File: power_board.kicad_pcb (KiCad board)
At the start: 2 copper layers, 156 x 90 mm, 110 parts, among them J1 Conn_01x01, J10 Conn_01x02, J11 Conn_01x02, J12 Conn_01x02, J13 Conn_01x02, J14 Conn_01x02, J15 Conn_01x02, J16 Conn_01x02, J17 Conn_01x02, J18 Conn_01x02, J19 Conn_01x02, J2 Conn_01x01, J20 Conn_01x03, J21 Conn_01x03, J22 Conn_01x03, J23 Conn_01x03, J24 Conn_01x03, J25 Conn_01x02, J26 Conn_01x02, J27 Conn_01x02, J28 Conn_01x02, J29 Conn_01x02, J3 Conn_01x01, J30 Conn_01x02, J4 ATX-24, J5 Conn_01x02, J6 Conn_01x02, J7 Conn_01x02, J8 Conn_01x02, J9 Conn_01x02, K1 SANYOU_SRD_Form_C, K2 SANYOU_SRD_Form_C, K3 SANYOU_SRD_Form_C, K4 SANYOU_SRD_Form_C, K5 SANYOU_SRD_Form_C, Q1 MMBT4401-7-F, Q10 MMBT4401-7-F, Q11 SI7113ADN-T1-GE3, Q12 Q_NMOS_GDS, Q13 Q_NMOS_GDS, Q14 Q_NMOS_GDS, Q15 Q_NMOS_GDS, Q16 Q_NMOS_GDS, Q2 MMBT4401-7-F, Q3 MMBT4401-7-F, Q4 SI7113ADN-T1-GE3, Q5 SI7113ADN-T1-GE3, Q6 MMBT4401-7-F, Q7 MMBT4401-7-F, Q8 SI7113ADN-T1-GE3, Q9 SI7113ADN-T1-GE3, U1 PCA9685PW, U2 PCA9685PW, U3 L298HN, U4 l6210, U5 L298HN, U6 l6210, U7 L298HN, U8 l6210

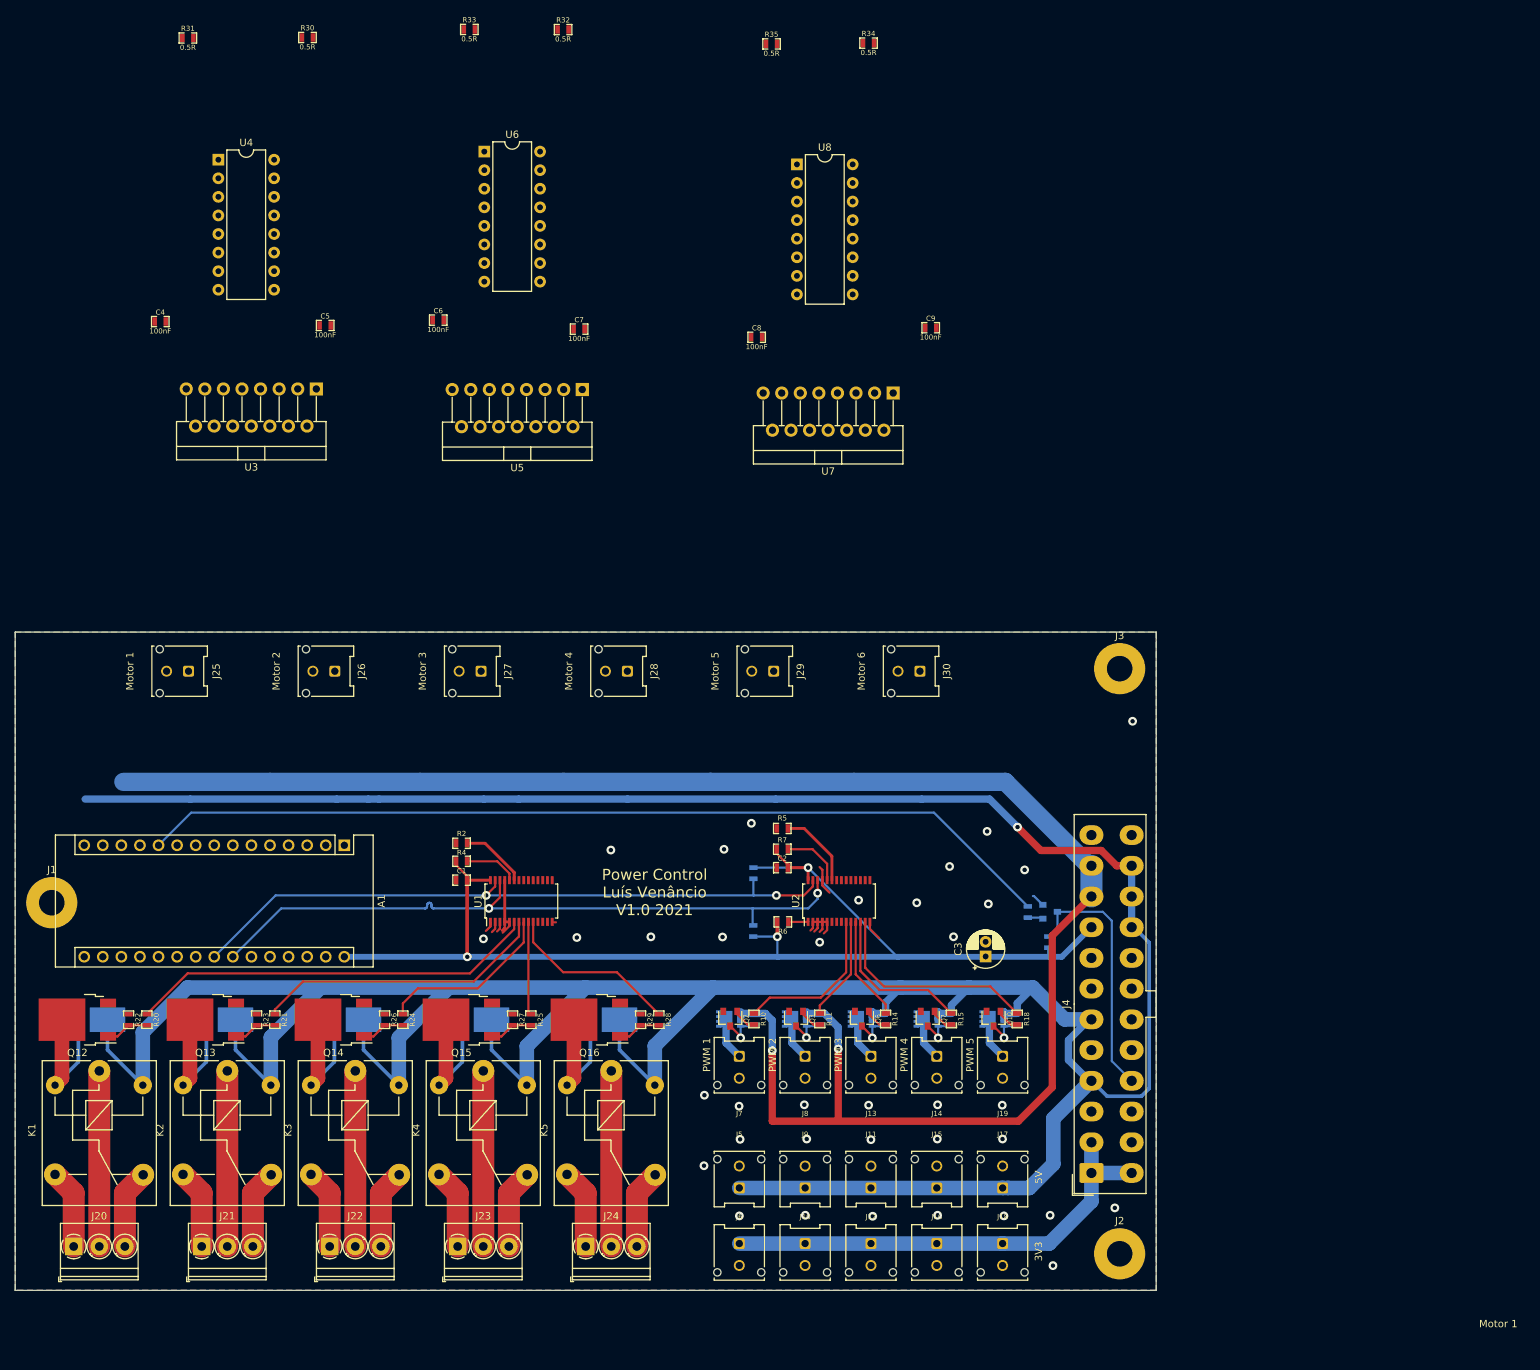
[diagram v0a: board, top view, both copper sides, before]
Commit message: Replaced driver footprints
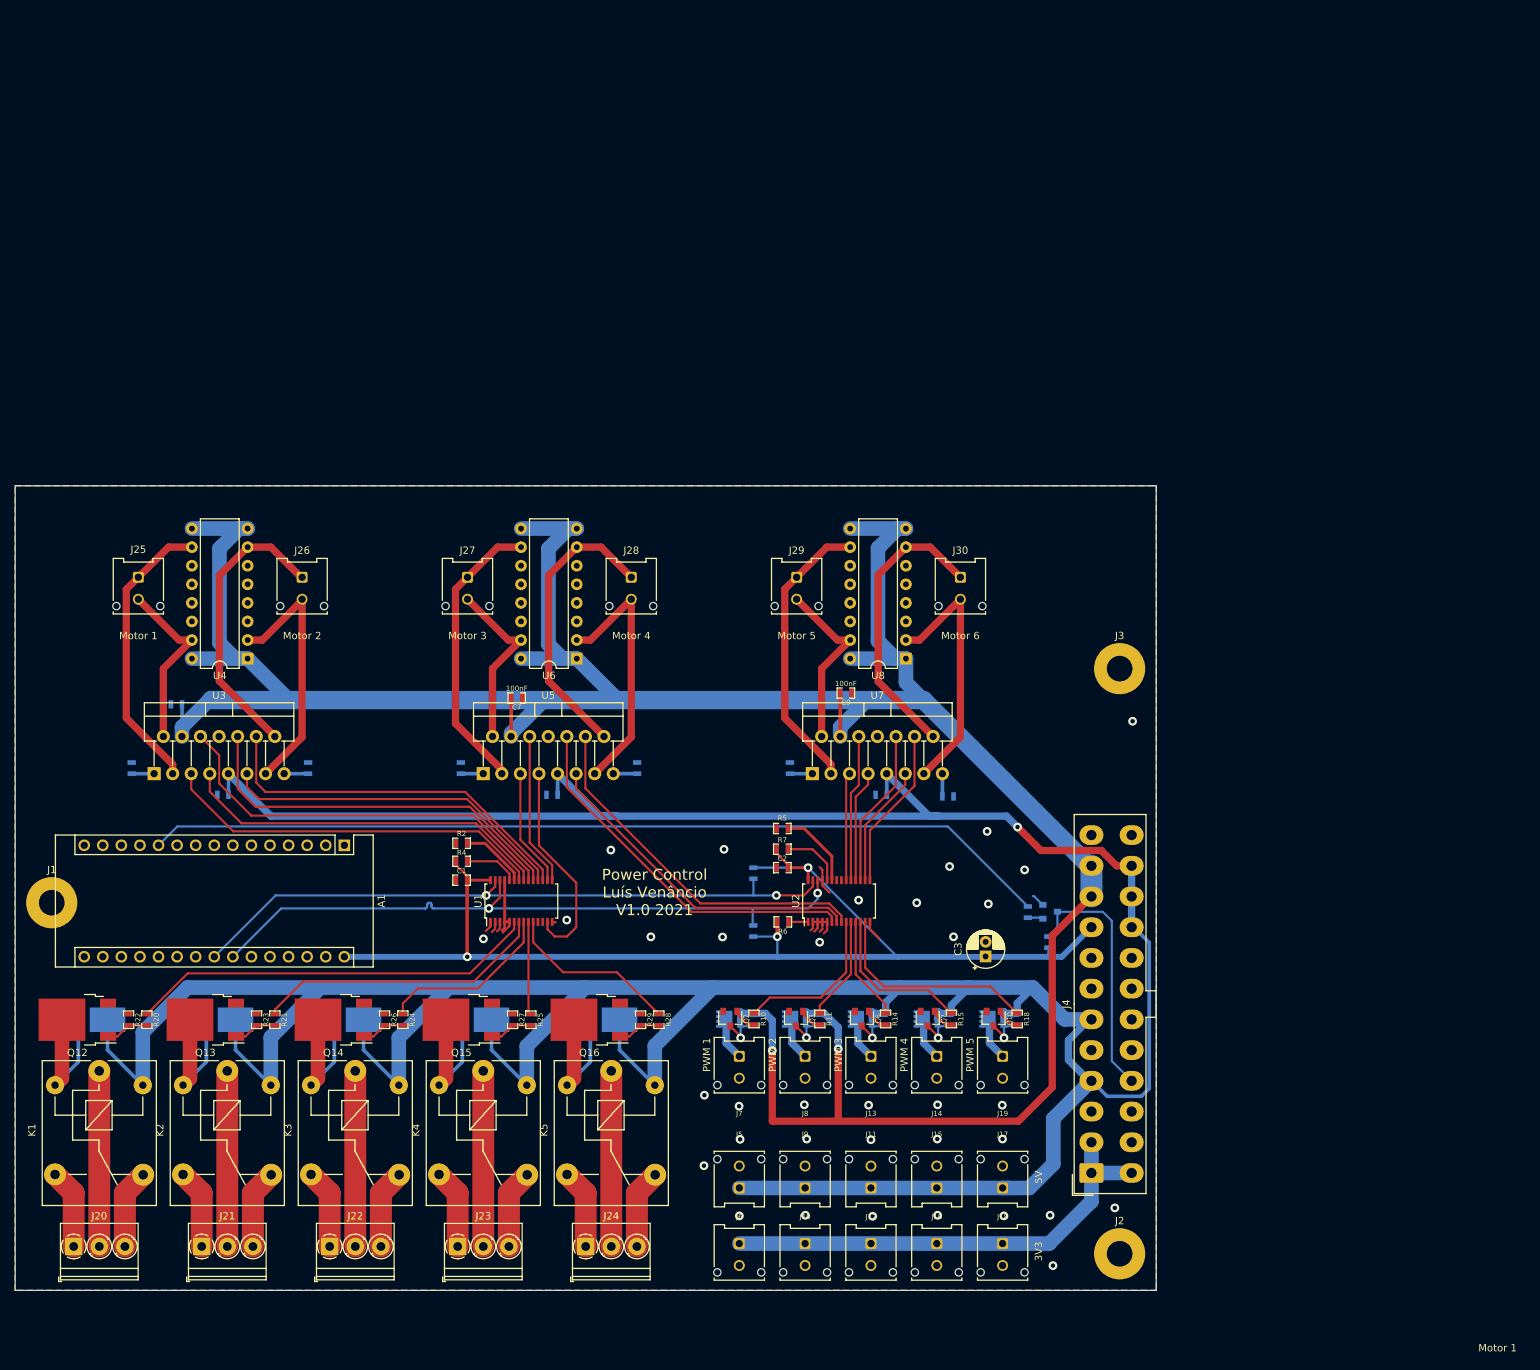
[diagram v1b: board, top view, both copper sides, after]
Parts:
- C4, C5, C6, C8, R30, R31, R32, R33, R34, R35: moved to B.Cu
- moved R35 105.7 mm to (192.5, 82.5)
- moved R33 103.6 mm to (150.0, 78.6), turned to 90 degrees
- moved R30 102.7 mm to (80.9, 78.6), turned to 90 degrees
- moved R32 101.9 mm to (125.9, 78.6), turned to 90 degrees
- moved R31 101.2 mm to (105.0, 78.6), turned to 90 degrees
- moved R34 99.7 mm to (170.9, 78.6), turned to 90 degrees
- moved U6 70.5 mm to (141.8, 63.6), turned to 180 degrees
- moved U8 69.2 mm to (186.8, 63.6), turned to 180 degrees
- moved U4 68.3 mm to (96.8, 63.6), turned to 180 degrees
- moved C6 66.7 mm to (138.4, 82.2), turned to 180 degrees
- moved C4 65.3 mm to (93.4, 82.2), turned to 180 degrees
- moved C8 64.8 mm to (183.4, 82.2), turned to 180 degrees
- moved U3 57.1 mm to (84.0, 79.4), turned to 0 degrees
- moved C5 55.7 mm to (87.0, 69.9)
- moved U5 54.2 mm to (129.0, 79.4), turned to 0 degrees
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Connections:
- U1 pad 11: /MTR3_IN1 -> Net-(U1-Pad11)
- U1 pad 12: /MTR3_IN2 -> Net-(U1-Pad12)
- U1 pad 13: /MTR3_EN -> /MTR3_IN2
- U1 pad 15: Net-(U1-Pad15) -> /MTR3_EN
- U1 pad 16: Net-(U1-Pad16) -> /MTR3_IN1
- U1 pad 17: /MTR2_EN -> /MTR2_IN2
- U1 pad 18: /MTR2_IN2 -> /MTR2_EN
- U2 pad 15: /MTR6_EN -> /MTR6_IN2
- U2 pad 16: /MTR6_IN2 -> /MTR6_EN
- U2 pad 18: /MTR5_EN -> /MTR5_IN2
- U2 pad 19: /MTR5_IN2 -> /MTR5_EN
- U2 pad 7: /MTR4_IN2 -> /MTR4_EN
- U2 pad 8: /MTR4_EN -> /MTR4_IN2
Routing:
- net +12V: track 248.3 -> 420.1 mm
- net /MTR1_EN: track 0.00 -> 56.0 mm
- net /MTR2_IN1: track 0.00 -> 53.5 mm
- net /MTR1_IN1: track 0.00 -> 52.8 mm
- net /MTR2_IN2: track 0.00 -> 51.9 mm
- net /MTR4_IN1: track 0.00 -> 51.2 mm
- net /MTR1_IN2: track 0.00 -> 51.1 mm
- net /MTR4_IN2: track 0.00 -> 50.1 mm
- net /MTR2_EN: track 0.00 -> 47.7 mm
- net /MTR4_EN: track 0.00 -> 45.7 mm
- net Net-(J26-Pad1): track 0.00 -> 39.9 mm
- net Net-(J28-Pad1): track 0.00 -> 39.8 mm
- net Net-(J30-Pad1): track 0.00 -> 39.7 mm
- net Net-(J25-Pad1): track 0.00 -> 39.2 mm
- net Net-(J27-Pad1): track 0.00 -> 39.2 mm
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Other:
- board size 156 x 90 mm -> 156 x 110 mm

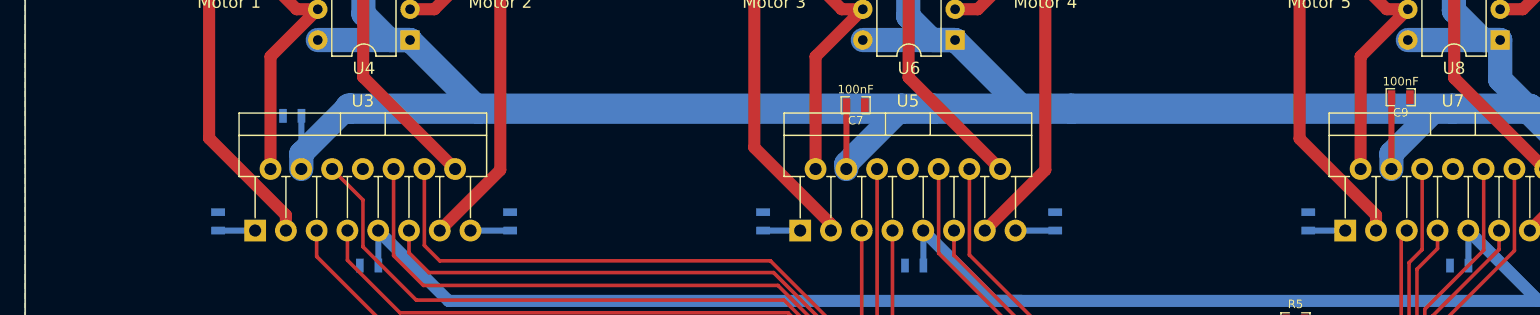
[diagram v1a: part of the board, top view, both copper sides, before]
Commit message: Added 220uf capacitors
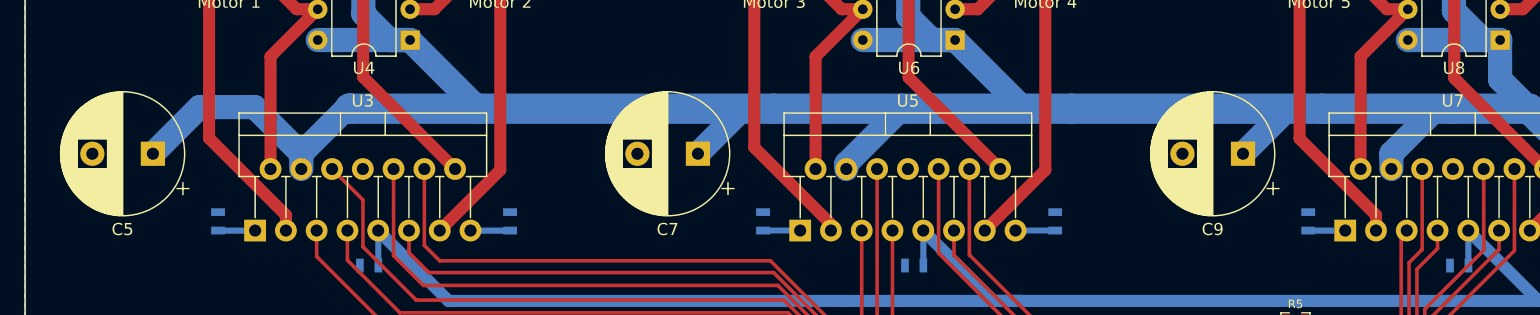
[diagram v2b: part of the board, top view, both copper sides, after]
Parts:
- C5: value 100nF -> 220uf; footprint lsts_passives:C_0603 -> Capacitor_THT:CP_Radial_D10.0mm_P5.00mm; moved to F.Cu
- C7, C9: value 100nF -> 220uf; footprint lsts_passives:C_0603 -> Capacitor_THT:CP_Radial_D10.0mm_P5.00mm
- moved C9 13.8 mm to (165.6, 73.0)
- moved C7 13.6 mm to (120.5, 73.0)
- moved C5 11.9 mm to (75.5, 73.0), turned to 180 degrees
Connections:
- C5 pad 1: GND -> +12V
- C5 pad 2: +12V -> GND
- C7 pad 1: GND -> +12V
- C7 pad 2: +12V -> GND
- C9 pad 1: GND -> +12V
- C9 pad 2: +12V -> GND
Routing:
- net +12V: track 420.1 -> 437.1 mm

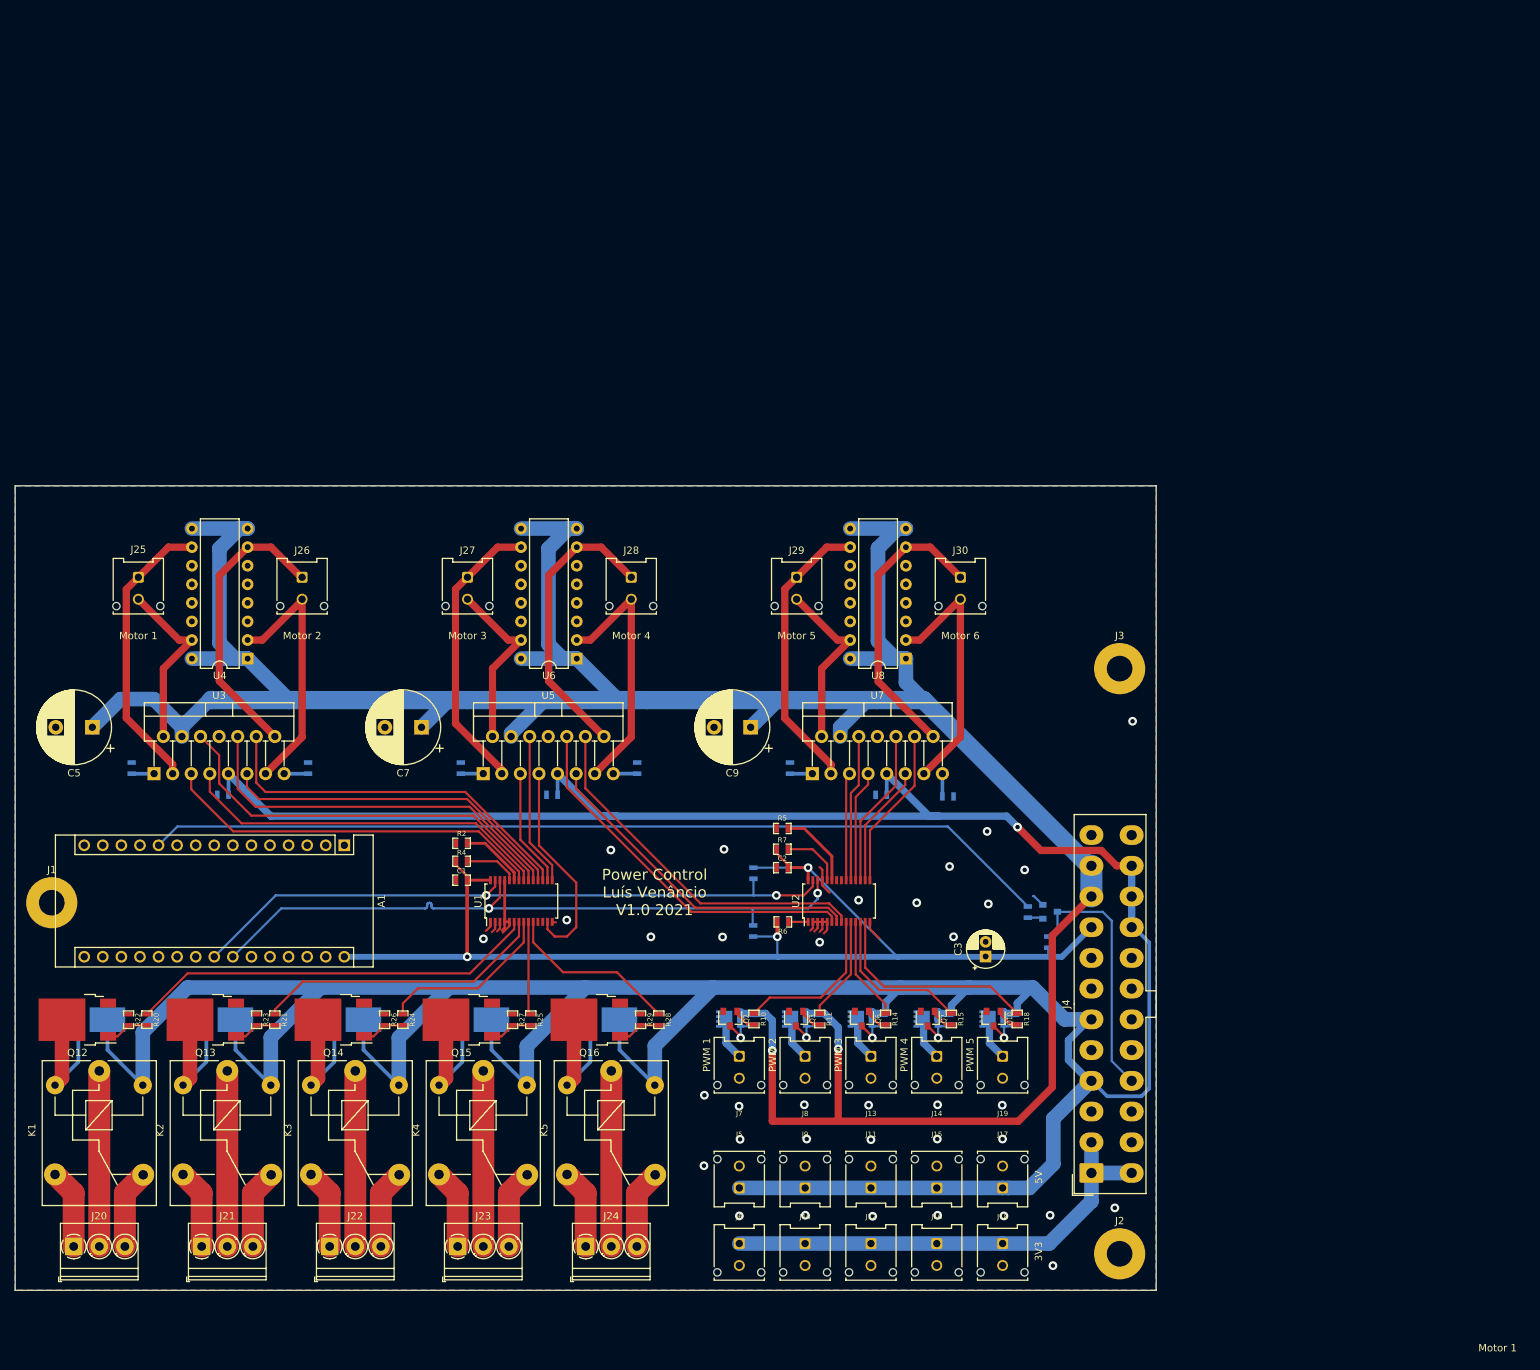
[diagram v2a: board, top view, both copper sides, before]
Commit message: Changed general footprint placement and added vias
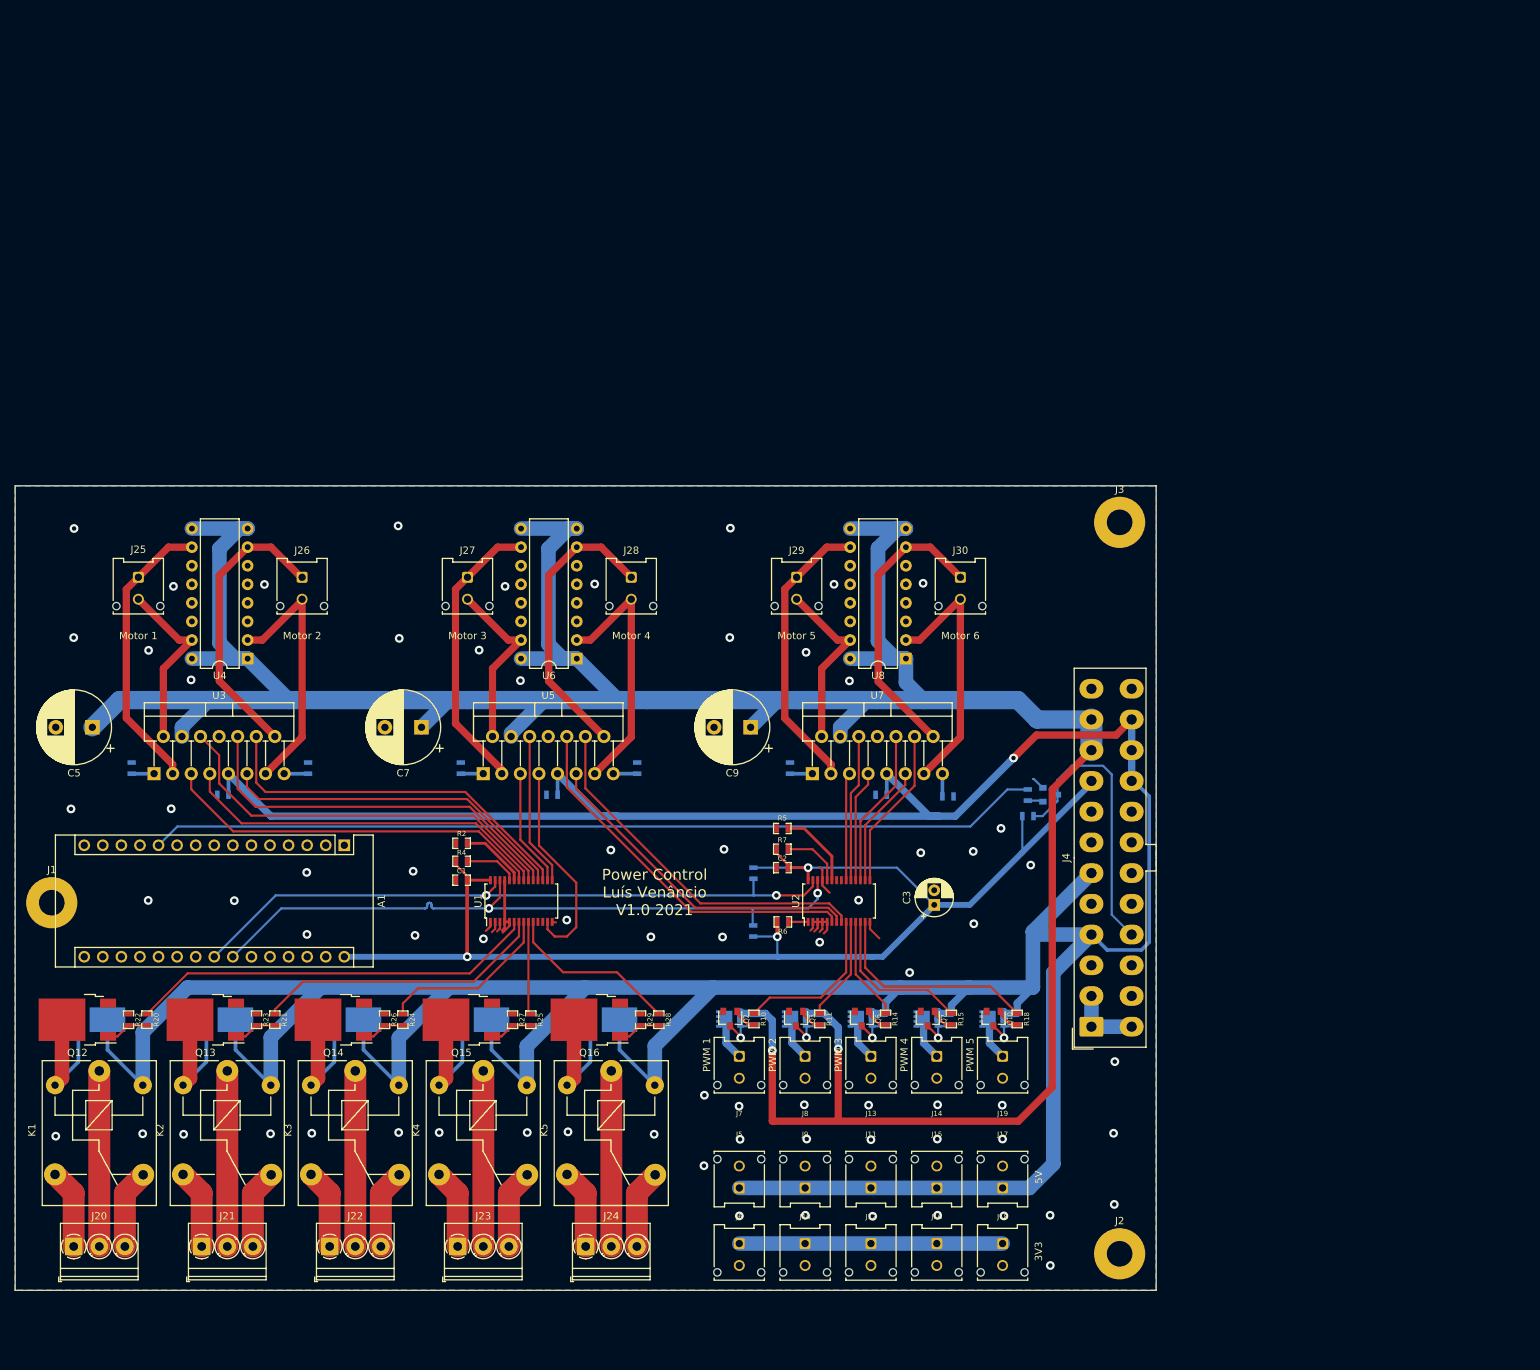
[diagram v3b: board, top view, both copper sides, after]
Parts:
- moved J3 20.0 mm to (216.0, 45.0)
- moved J4 20.0 mm to (212.1, 114.0)
- moved R9 17.5 mm to (203.5, 85.2), turned to 0 degrees
- moved Q1 16.0 mm to (206.5, 82.2)
- moved R8 16.0 mm to (203.4, 82.3)
- moved C3 9.95 mm to (190.7, 97.3)
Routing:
- net +5V: track 551.6 -> 580.1 mm
- net +3V3: track 64.1 -> 45.7 mm
- net /+5V_SB: track 162.8 -> 177.0 mm
- net +12V: track 437.1 -> 451.2 mm
- net Net-(J4-Pad16): track 34.9 -> 38.8 mm
- net /PWR_CTR: track 124.4 -> 122.0 mm
- net GND: vias 35 -> 72
